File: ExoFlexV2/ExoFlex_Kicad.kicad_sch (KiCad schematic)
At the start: 0 parts

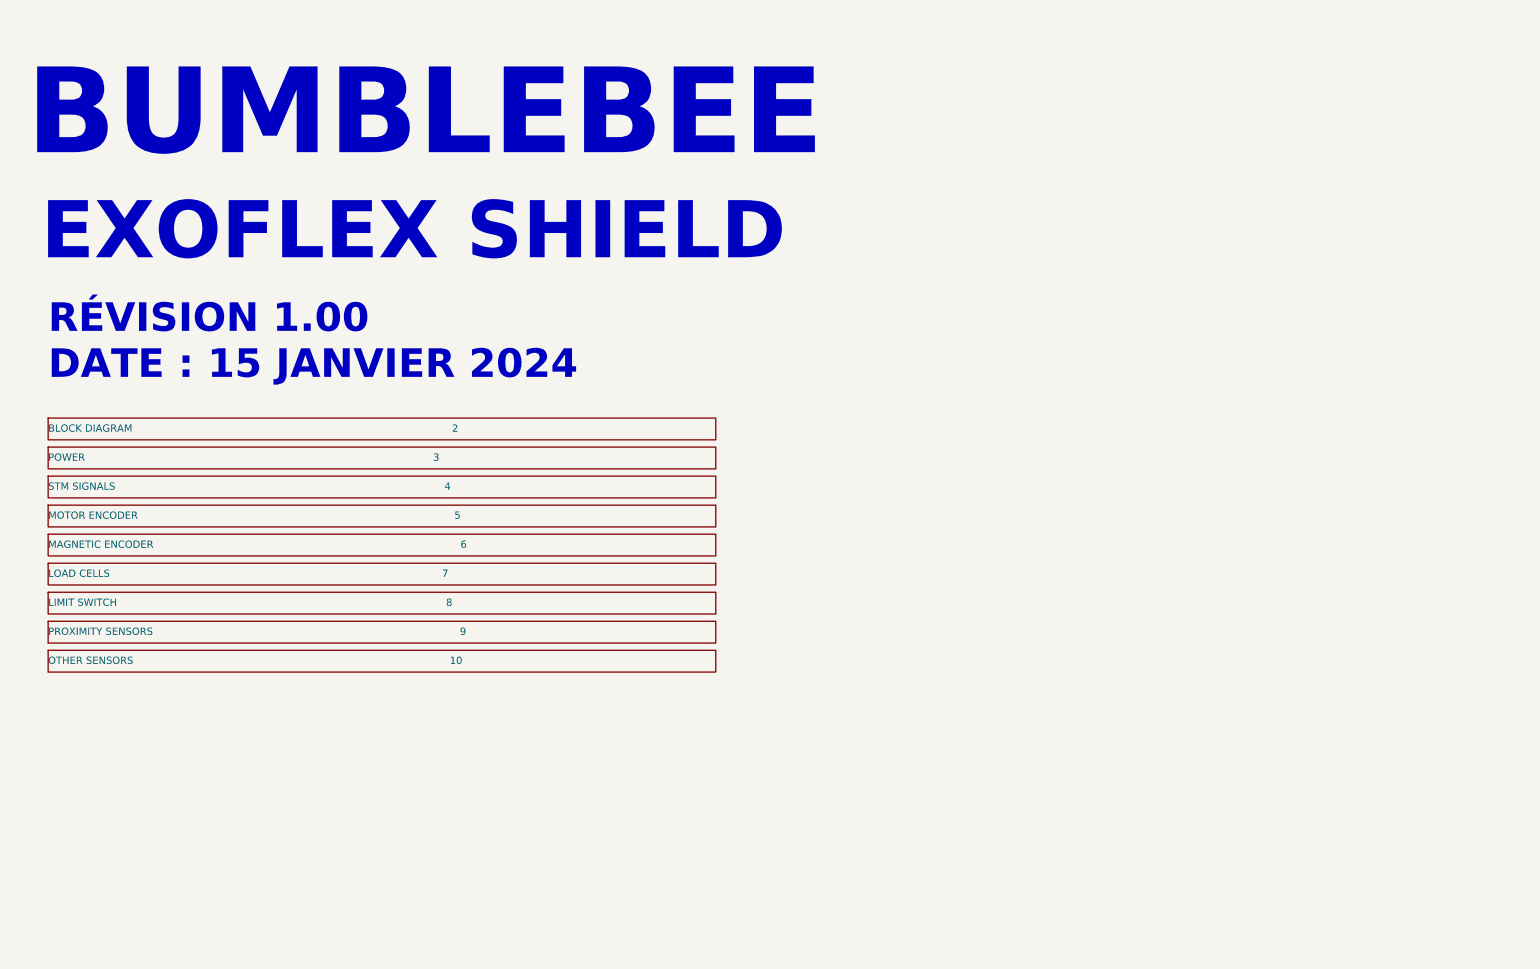
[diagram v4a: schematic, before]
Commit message: Many changes
Debouncing, power protection, potentiometer limits, etc.
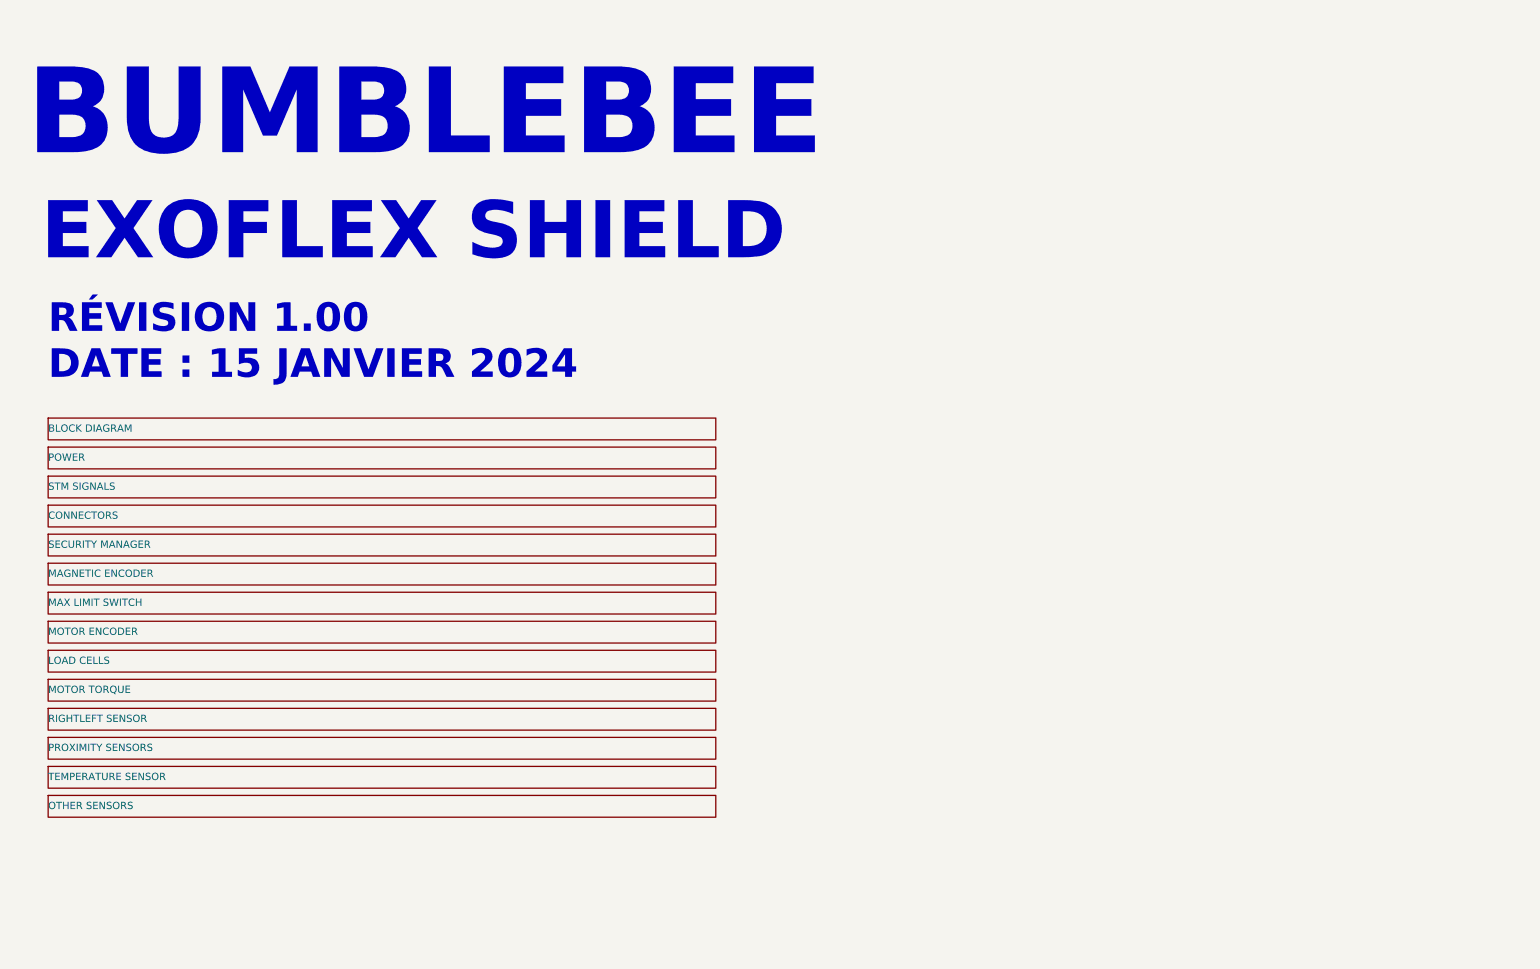
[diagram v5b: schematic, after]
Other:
- sheet BLOCK DIAGRAM                                                                                                     2 renamed BLOCK DIAGRAM
- sheet LIMIT SWITCH                                                                                                        8 renamed MAX LIMIT SWITCH
- sheet LOAD CELLS                                                                                                         7 renamed LOAD CELLS
- sheet MAGNETIC ENCODER                                                                                                 6 renamed MAGNETIC ENCODER
- sheet MOTOR ENCODER                                                                                                    5 renamed MOTOR ENCODER
- sheet OTHER SENSORS                                                                                                    10 renamed OTHER SENSORS
- sheet POWER                                                                                                              3 renamed POWER
- sheet STM SIGNALS                                                                                                        4 renamed STM SIGNALS
- removed sheet PROXIMITY SENSORS                                                                                                 9                                                                                       
- added sheet CONNECTORS (connectors.kicad_sch)
- added sheet MOTOR TORQUE (torque_motor.kicad_sch)
- added sheet PROXIMITY SENSORS (proximity_sensors.kicad_sch)
- added sheet RIGHTLEFT SENSOR (right_left_sensor.kicad_sch)
- added sheet SECURITY MANAGER (security_manager.kicad_sch)
- added sheet TEMPERATURE SENSOR (temperature_sensor.kicad_sch)
- sheet MAGNETIC ENCODER: file magneticencoder.kicad_sch -> magnetic_encoder_amplitude.kicad_sch
- sheet MAX LIMIT SWITCH: file sensors.kicad_sch -> limit_switch_amplitude.kicad_sch

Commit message: quque truc
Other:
- sheet LOAD CELLS renamed TORQUE SENSOR
